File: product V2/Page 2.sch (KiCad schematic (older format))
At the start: 9 parts, among them U3 ESP32-WROOM-32D

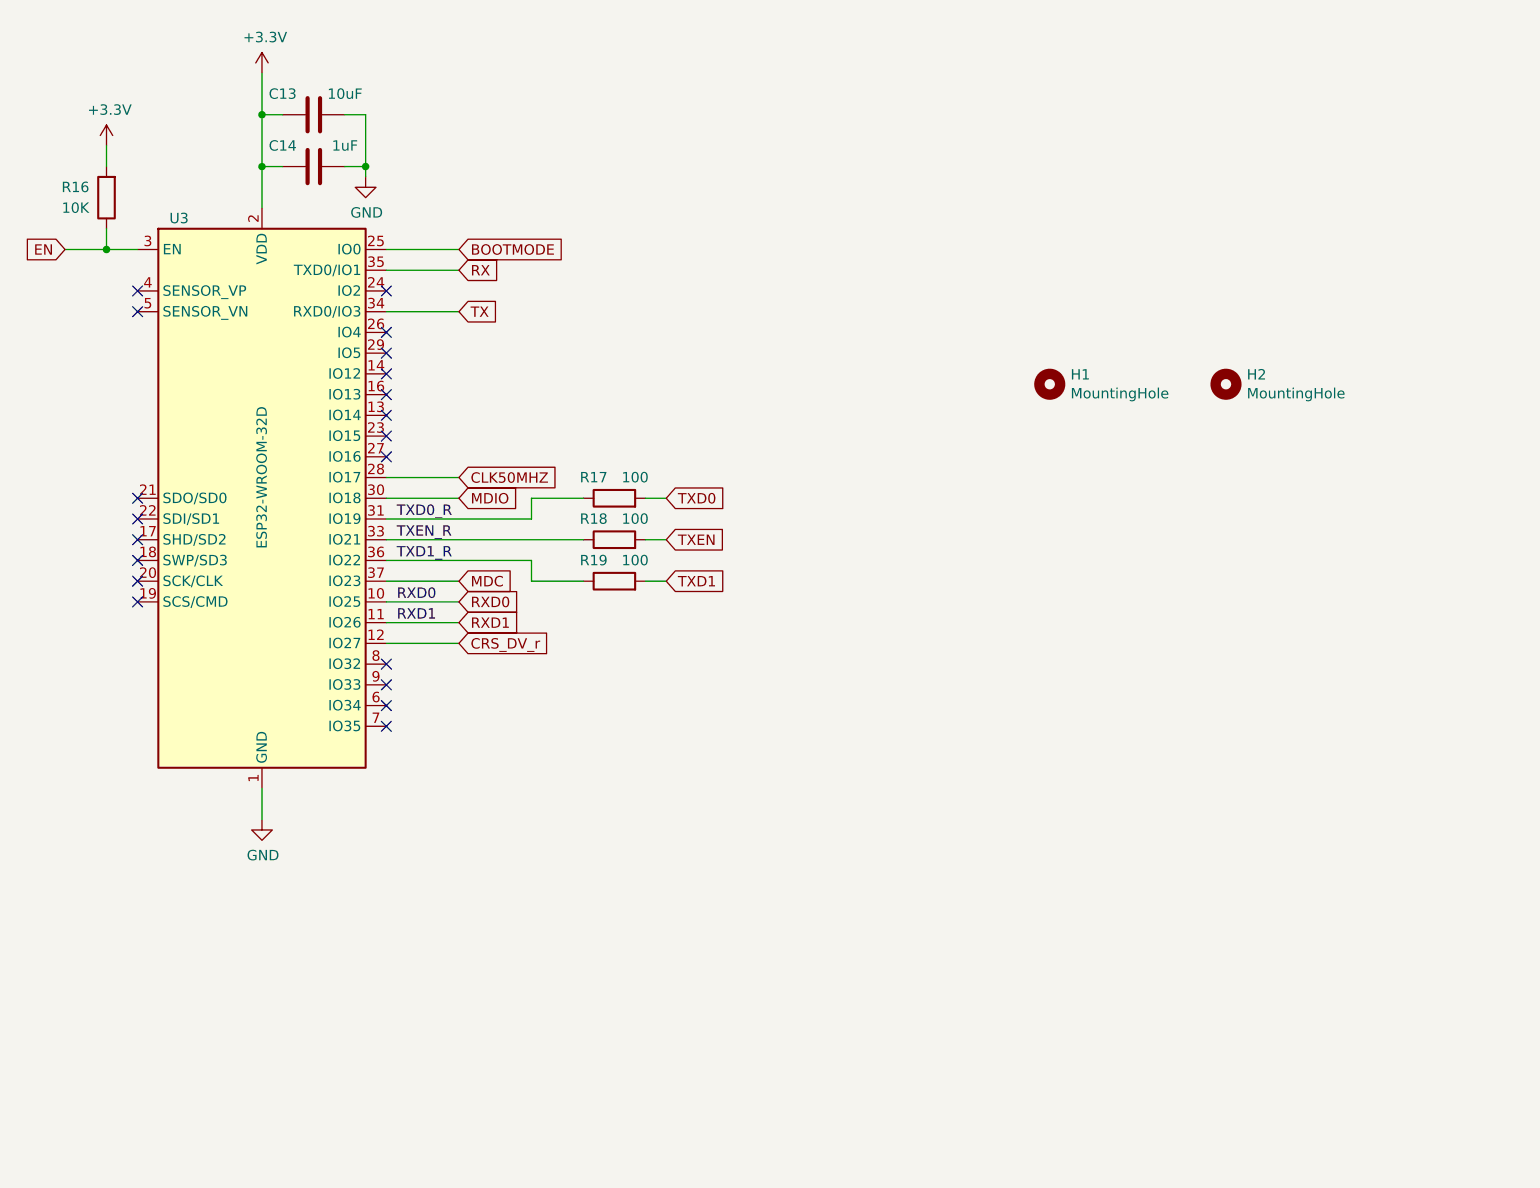
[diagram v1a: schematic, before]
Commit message: Started adding LEDs and pushbuttons to board
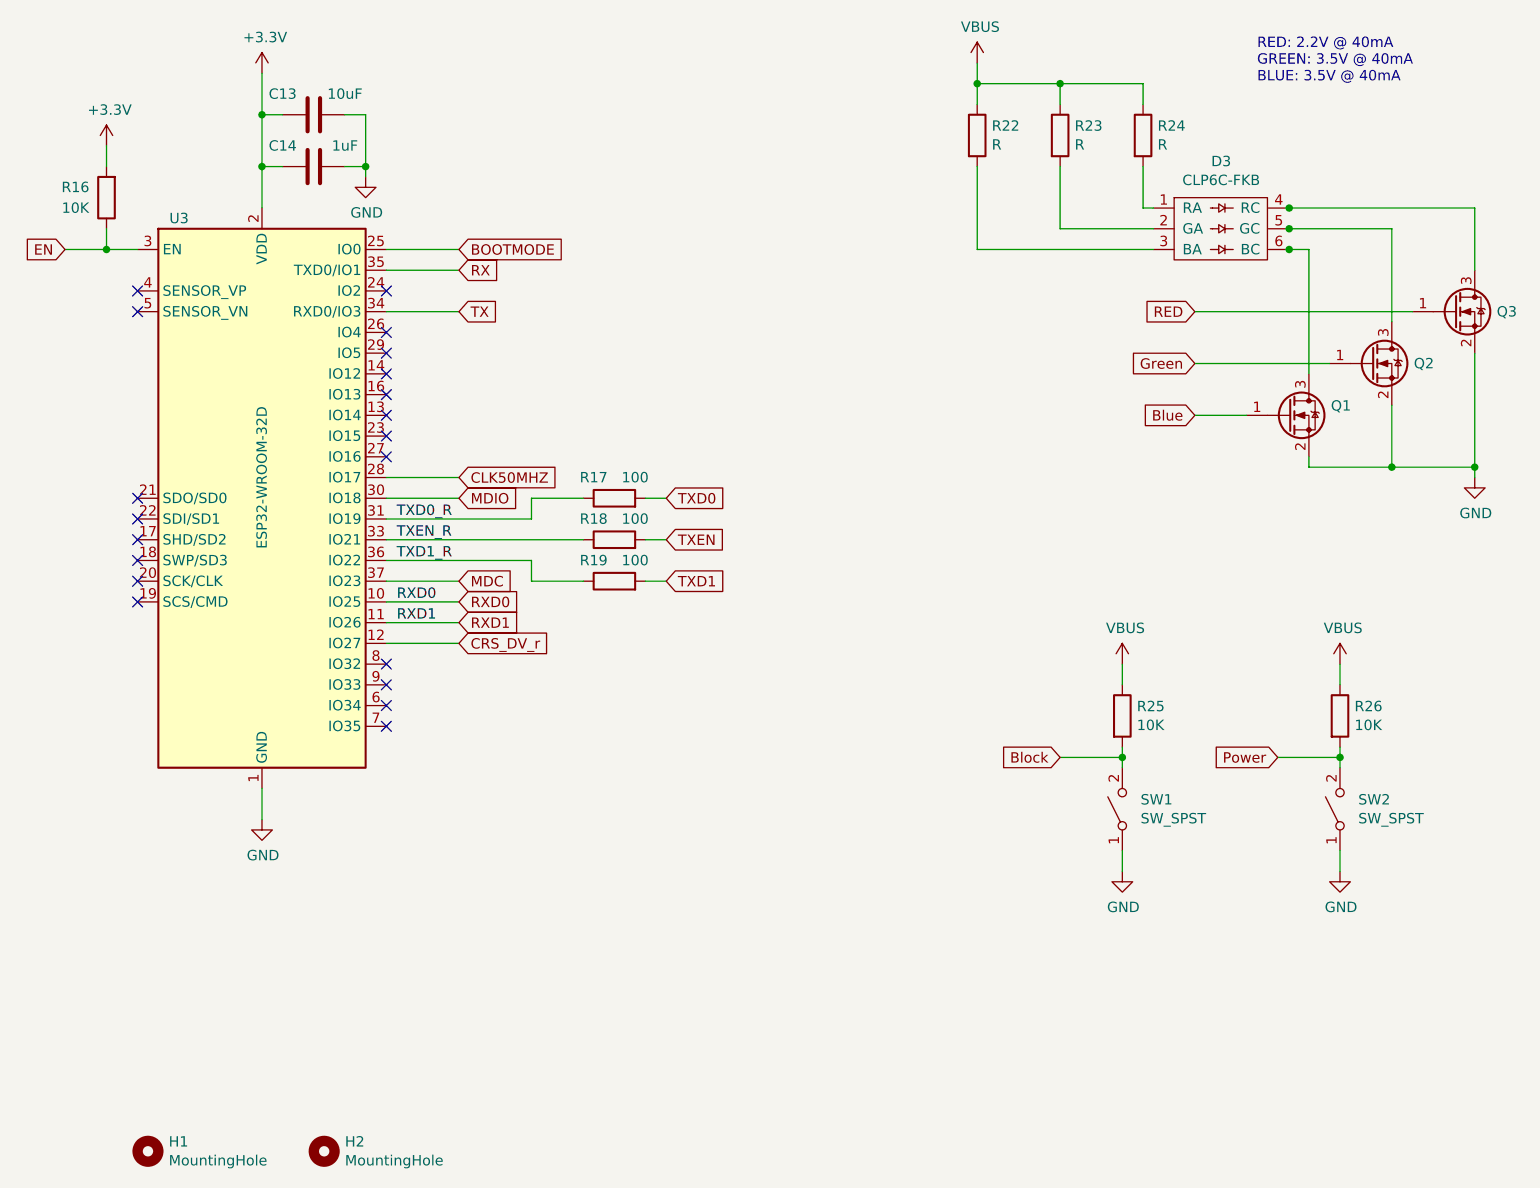
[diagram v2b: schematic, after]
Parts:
- added D3: CLP6C-FKB, My Footprints:CLP6C-FKB, symbol My_Symbols:CLP6C-FKB
- added Q1, Q2, Q3: Q_NMOS_GSD, symbol Device:Q_NMOS_GSD
- added R22, R23, R24: R, Resistor_SMD:R_0603_1608Metric, symbol Device:R
- added R25, R26: 10K, Resistor_SMD:R_0603_1608Metric, symbol Device:R
- added SW1, SW2: SW_SPST, symbol Switch:SW_SPST
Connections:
- net labels added: Block, Blue, Green, Power, RED, VBUS
- wire segments 33 -> 73
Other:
- note added: "RED: 2.2V @ 40mA\nGREEN: 3.5V @ 40mA\nBLUE: 3.5V @ 40mA\n"
- moved on the sheet: H1, H2

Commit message: Added block button and RGB LED
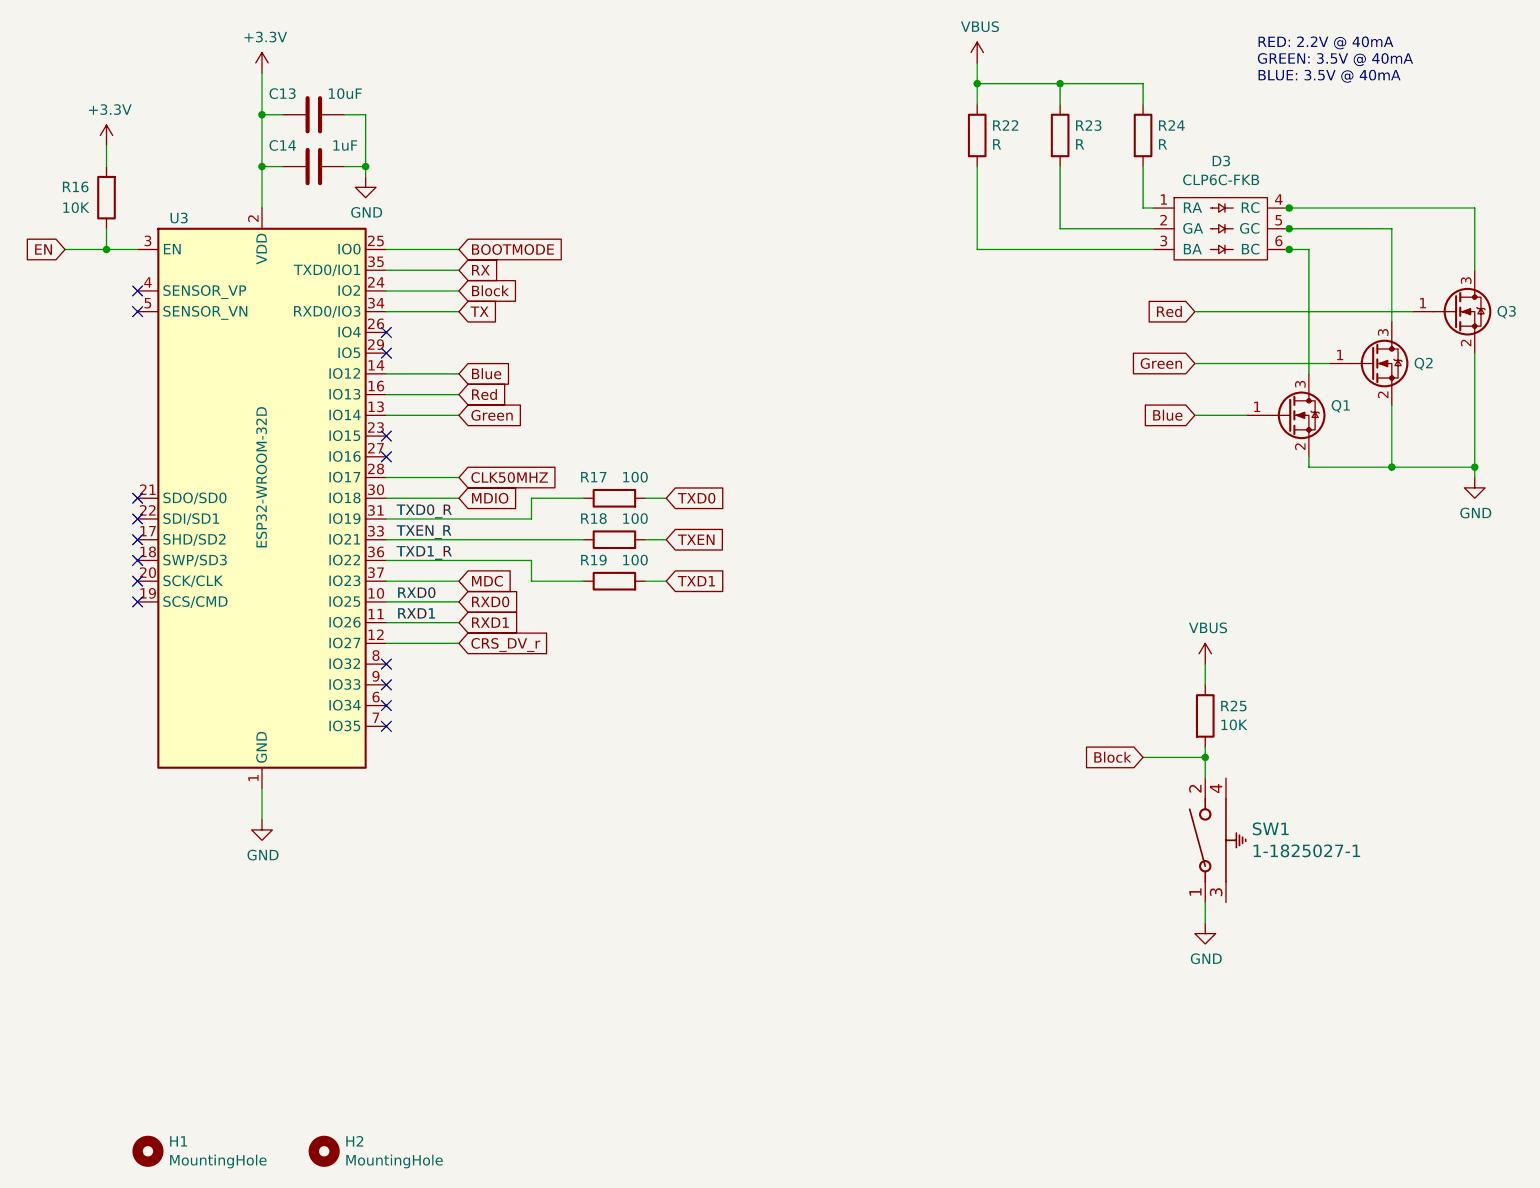
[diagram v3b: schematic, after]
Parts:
- removed R26: 10K, Resistor_SMD:R_0603_1608Metric, symbol Device:R
- removed SW1, SW2: SW_SPST, symbol Switch:SW_SPST
- added SW1: 1-1825027-1, 1-1825027-1:1-1825027-1, symbol 1-1825027-1:1-1825027-1
- H1, H2: footprint (none) -> MountingHole:MountingHole_2.2mm_M2_Pad
- Q1, Q2, Q3: footprint (none) -> digikey-footprints:SOT-23-3
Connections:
- net labels added: Red
- net labels removed: Power, RED
- wire segments 73 -> 72
- no-connect marks 20 -> 16
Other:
- moved on the sheet: R25
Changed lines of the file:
@@
 Wire Wire Line
 	4600 2650 4950 2650
-NoConn ~ 4600 2750
 NoConn ~ 4600 2950
 NoConn ~ 4600 3050
-NoConn ~ 4600 3150
 NoConn ~ 4600 3550
 Wire Wire Line
@@
 F 0 "H1" H 3550 6946 50  0000 L CNN
 F 1 "MountingHole" H 3550 6855 50  0000 L CNN
-F 2 "" H 3450 6900 50  0001 C CNN
+F 2 "MountingHole:MountingHole_2.2mm_M2_Pad" H 3450 6900 50  0001 C CNN
 F 3 "~" H 3450 6900 50  0001 C CNN
 	1    3450 6900
@@
 F 0 "H2" H 4400 6946 50  0000 L CNN
 F 1 "MountingHole" H 4400 6855 50  0000 L CNN
-F 2 "" H 4300 6900 50  0001 C CNN
+F 2 "MountingHole:MountingHole_2.2mm_M2_Pad" H 4300 6900 50  0001 C CNN
 F 3 "~" H 4300 6900 50  0001 C CNN
 	1    4300 6900
 	1    0    0    -1
 $EndComp
-NoConn ~ 4600 3250
-NoConn ~ 4600 3350
 NoConn ~ 4600 3450
 NoConn ~ 4600 4850
@@
 F 0 "Q1" H 9156 3396 50  0000 L CNN
 F 1 "Q_NMOS_GSD" H 9156 3305 50  0001 L CNN
-F 2 "" H 9150 3450 50  0001 C CNN
+F 2 "digikey-footprints:SOT-23-3" H 9150 3450 50  0001 C CNN
 F 3 "~" H 8950 3350 50  0001 C CNN
 	1    8950 3350
@@
 F 0 "Q2" H 9556 3100 50  0000 L CNN
 F 1 "Q_NMOS_GSD" H 9556 3055 50  0001 L CNN
-F 2 "" H 9550 3200 50  0001 C CNN
+F 2 "digikey-footprints:SOT-23-3" H 9550 3200 50  0001 C CNN
 F 3 "~" H 9350 3100 50  0001 C CNN
 	1    9350 3100
@@
 F 0 "Q3" H 9956 2850 50  0000 L CNN
 F 1 "Q_NMOS_GSD" H 9956 2805 50  0001 L CNN
-F 2 "" H 9950 2950 50  0001 C CNN
+F 2 "digikey-footprints:SOT-23-3" H 9950 2950 50  0001 C CNN
 F 3 "~" H 9750 2850 50  0001 C CNN
 	1    9750 2850
@@
 Green
 Text GLabel 8500 2850 0    50   Input ~ 0
-RED
+Red
 $Comp
 L power:VBUS #PWR?
 U 1 1 5F4D638B
-P 8150 4550
+P 8550 4550
 AR Path="/5F4D638B" Ref="#PWR?"  Part="1"
 AR Path="/5DED2F9B/5F4D638B" Ref="#PWR?"  Part="1"
 AR Path="/5DED3446/5F4D638B" Ref="#PWR0135"  Part="1"
-F 0 "#PWR0135" H 8150 4400 50  0001 C CNN
-F 1 "VBUS" H 8165 4723 50  0000 C CNN
-F 2 "" H 8150 4550 50  0001 C CNN
-F 3 "" H 8150 4550 50  0001 C CNN
-	1    8150 4550
+F 0 "#PWR0135" H 8550 4400 50  0001 C CNN
+F 1 "VBUS" H 8565 4723 50  0000 C CNN
+F 2 "" H 8550 4550 50  0001 C CNN
+F 3 "" H 8550 4550 50  0001 C CNN
+	1    8550 4550
 	1    0    0    -1
 $EndComp
@@
 L Device:R R25
 U 1 1 5F4D639E
-P 8150 4800
-F 0 "R25" H 8220 4846 50  0000 L CNN
-F 1 "10K" H 8220 4755 50  0000 L CNN
-F 2 "Resistor_SMD:R_0603_1608Metric" V 8080 4800 50  0001 C CNN
-F 3 "~" H 8150 4800 50  0001 C CNN
-	1    8150 4800
-	1    0    0    -1
-$EndComp
-$Comp
-L Switch:SW_SPST SW1
-U 1 1 5F4DB73B
-P 8150 5250
-F 0 "SW1" V 8196 5162 50  0000 R CNN
-F 1 "SW_SPST" V 8105 5162 50  0000 R CNN
-F 2 "" H 8150 5250 50  0001 C CNN
-F 3 "~" H 8150 5250 50  0001 C CNN
-	1    8150 5250
-	0    -1   -1   0
+P 8550 4800
+F 0 "R25" H 8620 4846 50  0000 L CNN
+F 1 "10K" H 8620 4755 50  0000 L CNN
+F 2 "Resistor_SMD:R_0603_1608Metric" V 8480 4800 50  0001 C CNN
+F 3 "~" H 8550 4800 50  0001 C CNN
+	1    8550 4800
+	1    0    0    -1
 $EndComp
 $Comp
 L power:GND #PWR0136
 U 1 1 5F4DC54A
-P 8150 5550
-F 0 "#PWR0136" H 8150 5300 50  0001 C CNN
-F 1 "GND" H 8155 5377 50  0000 C CNN
-F 2 "" H 8150 5550 50  0001 C CNN
-F 3 "" H 8150 5550 50  0001 C CNN
-	1    8150 5550
-	1    0    0    -1
-$EndComp
-Wire Wire Line
-	8150 5450 8150 5550
-Wire Wire Line
-	8150 5050 8150 5000
-Wire Wire Line
-	8150 4650 8150 4550
-Wire Wire Line
-	8150 5000 7850 5000
-Connection ~ 8150 5000
-Wire Wire Line
-	8150 5000 8150 4950
-Text GLabel 7850 5000 0    50   Input ~ 0
+P 8550 5800
+F 0 "#PWR0136" H 8550 5550 50  0001 C CNN
+F 1 "GND" H 8555 5627 50  0000 C CNN
+F 2 "" H 8550 5800 50  0001 C CNN
+F 3 "" H 8550 5800 50  0001 C CNN
+	1    8550 5800
+	1    0    0    -1
+$EndComp
+Wire Wire Line
+	8550 5700 8550 5800
+Wire Wire Line
+	8550 4650 8550 4550
+Wire Wire Line
+	8550 5000 8250 5000
+Connection ~ 8550 5000
+Wire Wire Line
+	8550 5000 8550 4950
+Text GLabel 8250 5000 0    50   Input ~ 0
 Block
-$Comp
-L power:VBUS #PWR?
-U 1 1 5F4E308B
-P 9200 4550
-AR Path="/5F4E308B" Ref="#PWR?"  Part="1"
-AR Path="/5DED2F9B/5F4E308B" Ref="#PWR?"  Part="1"
-AR Path="/5DED3446/5F4E308B" Ref="#PWR0137"  Part="1"
-F 0 "#PWR0137" H 9200 4400 50  0001 C CNN
-F 1 "VBUS" H 9215 4723 50  0000 C CNN
-F 2 "" H 9200 4550 50  0001 C CNN
-F 3 "" H 9200 4550 50  0001 C CNN
-	1    9200 4550
-	1    0    0    -1
-$EndComp
-$Comp
-L Device:R R26
-U 1 1 5F4E3091
-P 9200 4800
-F 0 "R26" H 9270 4846 50  0000 L CNN
-F 1 "10K" H 9270 4755 50  0000 L CNN
-F 2 "Resistor_SMD:R_0603_1608Metric" V 9130 4800 50  0001 C CNN
-F 3 "~" H 9200 4800 50  0001 C CNN
-	1    9200 4800
-	1    0    0    -1
-$EndComp
-$Comp
-L Switch:SW_SPST SW2
-U 1 1 5F4E3097
-P 9200 5250
-F 0 "SW2" V 9246 5162 50  0000 R CNN
-F 1 "SW_SPST" V 9155 5162 50  0000 R CNN
-F 2 "" H 9200 5250 50  0001 C CNN
-F 3 "~" H 9200 5250 50  0001 C CNN
-	1    9200 5250
-	0    -1   -1   0
-$EndComp
-$Comp
-L power:GND #PWR0138
-U 1 1 5F4E309D
-P 9200 5550
-F 0 "#PWR0138" H 9200 5300 50  0001 C CNN
-F 1 "GND" H 9205 5377 50  0000 C CNN
-F 2 "" H 9200 5550 50  0001 C CNN
-F 3 "" H 9200 5550 50  0001 C CNN
-	1    9200 5550
-	1    0    0    -1
-$EndComp
-Wire Wire Line
-	9200 5450 9200 5550
-Wire Wire Line
-	9200 5050 9200 5000
-Wire Wire Line
-	9200 4650 9200 4550
-Wire Wire Line
-	9200 5000 8900 5000
-Connection ~ 9200 5000
-Wire Wire Line
-	9200 5000 9200 4950
-Text GLabel 8900 5000 0    50   Input ~ 0
-Power
 Text Notes 8800 1750 0    50   ~ 0
 RED: 2.2V @ 40mA\nGREEN: 3.5V @ 40mA\nBLUE: 3.5V @ 40mA\n
@@
 Wire Wire Line
 	8955 2350 9850 2350
+$Comp
+L 1-1825027-1:1-1825027-1 SW1
+U 1 1 5F4EC3B1
+P 8550 5400
+F 0 "SW1" V 8603 5176 60  0000 R CNN
+F 1 "1-1825027-1" V 8497 5176 60  0000 R CNN
+F 2 "1-1825027-1:1-1825027-1" H 8550 5215 60  0001 C CNN
+F 3 "" H 8550 5400 60  0000 C CNN
+	1    8550 5400
+	0    -1   -1   0
+$EndComp
+Wire Wire Line
+	8550 5000 8550 5100
+Wire Wire Line
+	4600 3150 4950 3150
+Wire Wire Line
+	4600 3250 4950 3250
+Wire Wire Line
+	4600 3350 4950 3350
+Text GLabel 4950 3150 2    50   Input ~ 0
+Blue
+Text GLabel 4950 3250 2    50   Input ~ 0
+Red
+Text GLabel 4950 3350 2    50   Input ~ 0
+Green
+Wire Wire Line
+	4600 2750 4950 2750
+Text GLabel 4950 2750 2    50   Input ~ 0
+Block
 $EndSCHEMATC

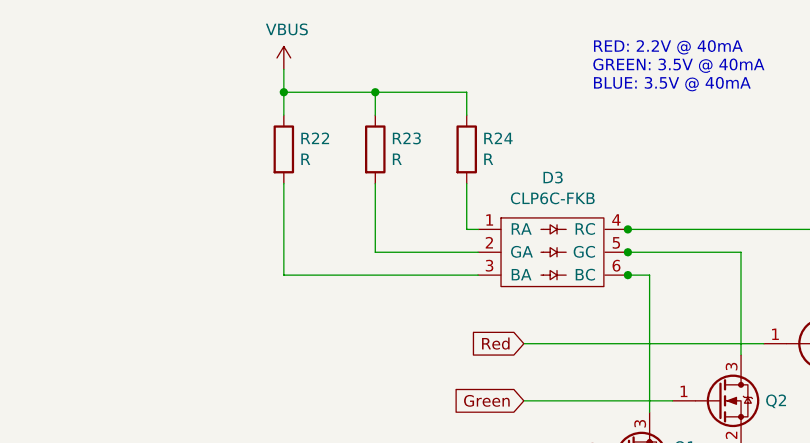
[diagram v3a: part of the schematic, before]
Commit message: Added buttons and LEDs
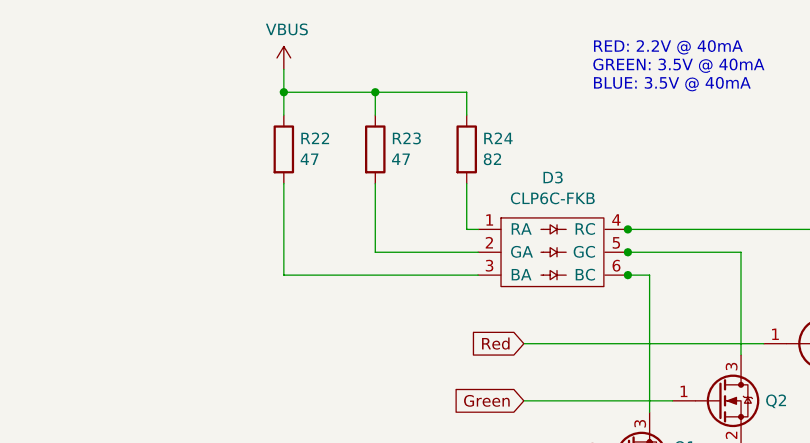
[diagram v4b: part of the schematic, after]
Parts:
- R22, R23: value R -> 47
- R24: value R -> 82
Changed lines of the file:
@@
 P 8250 2000
 F 0 "R24" H 8320 2046 50  0000 L CNN
-F 1 "R" H 8320 1955 50  0000 L CNN
+F 1 "82" H 8320 1955 50  0000 L CNN
 F 2 "Resistor_SMD:R_0603_1608Metric" V 8180 2000 50  0001 C CNN
 F 3 "~" H 8250 2000 50  0001 C CNN
@@
 P 7850 2000
 F 0 "R23" H 7920 2046 50  0000 L CNN
-F 1 "R" H 7920 1955 50  0000 L CNN
+F 1 "47" H 7920 1955 50  0000 L CNN
 F 2 "Resistor_SMD:R_0603_1608Metric" V 7780 2000 50  0001 C CNN
 F 3 "~" H 7850 2000 50  0001 C CNN
@@
 P 7450 2000
 F 0 "R22" H 7520 2046 50  0000 L CNN
-F 1 "R" H 7520 1955 50  0000 L CNN
+F 1 "47" H 7520 1955 50  0000 L CNN
 F 2 "Resistor_SMD:R_0603_1608Metric" V 7380 2000 50  0001 C CNN
 F 3 "~" H 7450 2000 50  0001 C CNN
